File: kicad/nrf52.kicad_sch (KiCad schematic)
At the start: 22 parts, among them U1005 NRF52833-CJAA, Y1001 ECS-320-8-47B-7KM-TR, Y1002 Crystal

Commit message: unify module and board
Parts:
- renumbered AE1001 to AE1, C1014 to C46, C1015 to C47, C1016 to C48, C1017 to C49, C1018 to C50, C1019 to C51, C1020 to C52, C1021 to C53, C1022 to C54, C1023 to C55, C1024 to C56, C1025 to C57, C1026 to C58, C1027 to C59, C1028 to C60, L1003 to L3, L1004 to L4, L1005 to L5, U1005 to U15, Y1001 to Y3, Y1002 to Y4

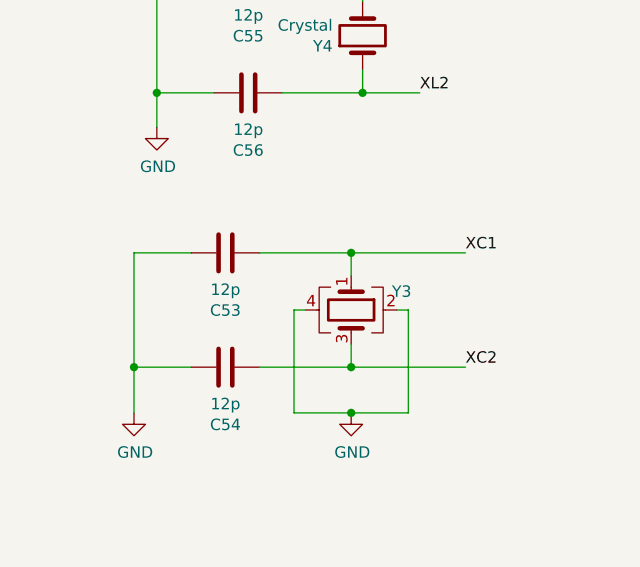
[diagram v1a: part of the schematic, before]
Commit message: move module parts to common library
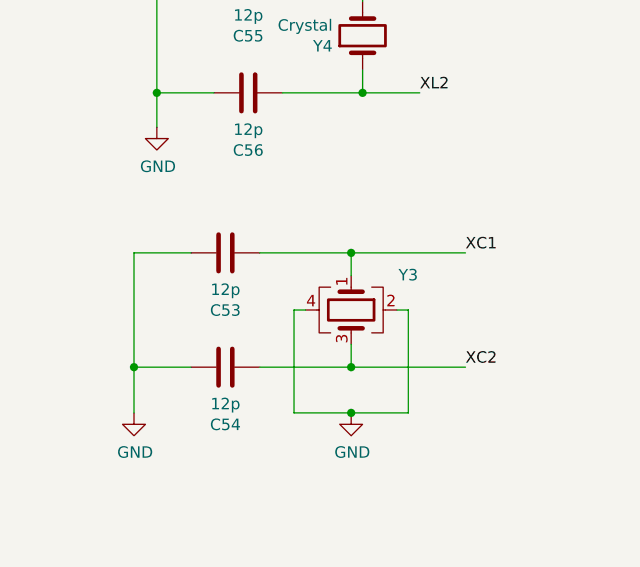
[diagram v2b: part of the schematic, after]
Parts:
- U15: symbol Riotee:NRF52833-CJAA -> riotee:NRF52833-CJAA
- Y3: symbol Riotee:ECS-320-8-47B-7KM-TR -> riotee:ECS-320-8-47B-7KM-TR
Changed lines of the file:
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@@
 	)
 	(symbol
-		(lib_id "Riotee:ECS-320-8-47B-7KM-TR")
+		(lib_id "riotee:ECS-320-8-47B-7KM-TR")
 		(at 255.27 59.69 270)
 		(unit 1)
@@
 		(fields_autoplaced yes)
 		(property "Reference" "Y3"
-			(at 260.8829 57.638 90)
+			(at 261.62 55.8098 90)
 			(effects
 				(font
@@
 			)
 		)
-		(property "Description" "32MHz, 8pF, 50R Crystal"
+		(property "Description" "Four pin crystal, GND on pins 2 and 4"
 			(at 255.27 59.69 0)
 			(effects
@@
 	)
 	(symbol
-		(lib_id "Riotee:NRF52833-CJAA")
+		(lib_id "riotee:NRF52833-CJAA")
 		(at 119.38 86.36 0)
 		(unit 1)

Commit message: resolve ERC
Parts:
- AE1: footprint Riotee:Texas_SWRA117D_2.4GHz_Left -> riotee:Texas_SWRA117D_2.4GHz_Left
- C46: footprint Riotee:C_0402_1005Metric -> riotee:C_0402_1005Metric; symbol Riotee:C -> Device:C
- C47, C48, C49, C50, C52, C53, C54, C55, C56, C58, C60: footprint Riotee:C_0201_0603Metric -> riotee:C_0201_0603Metric; symbol Riotee:C -> Device:C
- C51, C57, C59: footprint Riotee:RFSMD_0201_0603Metric -> riotee:RFSMD_0201_0603Metric; symbol Riotee:C -> Device:C
- L3, L4, L5: footprint Riotee:RFSMD_0201_0603Metric -> riotee:RFSMD_0201_0603Metric
- U15: footprint Riotee:NRF52833-CJAA -> riotee:NRF52833-CJAA
- Y3: footprint Riotee:ECS_ECX-1247B -> riotee:ECS_ECX-1247B
- Y4: footprint Riotee:ECX-12R -> riotee:ECX-12R

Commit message: resolve remaining import errors
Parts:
- C46: footprint riotee:C_0402_1005Metric -> Capacitor_SMD:C_0402_1005Metric
- C47, C48, C49, C50, C52, C53, C54, C55, C56, C58, C60: footprint riotee:C_0201_0603Metric -> Capacitor_SMD:C_0201_0603Metric
- L3, L4, L5: symbol Riotee:L -> Device:L
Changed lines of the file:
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@@
 	)
 	(symbol
-		(lib_id "Riotee:L")
+		(lib_id "Device:L")
 		(at 227.33 143.51 270)
 		(unit 1)
@@
 			)
 		)
-		(property "Datasheet" ""
+		(property "Datasheet" "~"
 			(at 227.33 143.51 0)
 			(effects
@@
 			)
 		)
-		(property "Description" "FIXED IND 5.6NH 350MA 400MOHM SM"
+		(property "Description" "Inductor"
 			(at 227.33 143.51 0)
 			(effects
@@
 			)
 		)
-		(property "Footprint" "riotee:C_0201_0603Metric"
+		(property "Footprint" "Capacitor_SMD:C_0201_0603Metric"
 			(at 61.2648 44.45 0)
 			(effects
@@
 			)
 		)
-		(property "Footprint" "riotee:C_0201_0603Metric"
+		(property "Footprint" "Capacitor_SMD:C_0201_0603Metric"
 			(at 237.49 54.3052 0)
 			(effects
@@
 			)
 		)
-		(property "Footprint" "riotee:C_0201_0603Metric"
+		(property "Footprint" "Capacitor_SMD:C_0201_0603Metric"
 			(at 237.49 67.0052 0)
 			(effects
@@
 			)
 		)
-		(property "Footprint" "riotee:C_0201_0603Metric"
+		(property "Footprint" "Capacitor_SMD:C_0201_0603Metric"
 			(at 240.03 23.8252 0)
 			(effects
@@
 			)
 		)
-		(property "Footprint" "riotee:C_0402_1005Metric"
+		(property "Footprint" "Capacitor_SMD:C_0402_1005Metric"
 			(at 21.2852 52.07 0)
 			(effects
@@
 			)
 		)
-		(property "Footprint" "riotee:C_0201_0603Metric"
+		(property "Footprint" "Capacitor_SMD:C_0201_0603Metric"
 			(at 51.1048 44.45 0)
 			(effects
@@
 			)
 		)
-		(property "Footprint" "riotee:C_0201_0603Metric"
+		(property "Footprint" "Capacitor_SMD:C_0201_0603Metric"
 			(at 254.3048 105.41 0)
 			(effects
@@
 	)
 	(symbol
-		(lib_id "Riotee:L")
+		(lib_id "Device:L")
 		(at 242.57 148.59 0)
 		(unit 1)
@@
 			)
 		)
-		(property "Datasheet" ""
+		(property "Datasheet" "~"
 			(at 242.57 148.59 0)
 			(effects
@@
 			)
 		)
-		(property "Description" "FIXED IND 2.7NH 500MA 200MOHM SM"
+		(property "Description" "Inductor"
 			(at 242.57 148.59 0)
 			(effects
@@
 			)
 		)
-		(property "Footprint" "riotee:C_0201_0603Metric"
+		(property "Footprint" "Capacitor_SMD:C_0201_0603Metric"
 			(at 40.9448 44.45 0)
 			(effects
@@
 	)
 	(symbol
-		(lib_id "Riotee:L")
+		(lib_id "Device:L")
 		(at 215.9 143.51 270)
 		(unit 1)
@@
 			)
 		)
-		(property "Datasheet" ""
+		(property "Datasheet" "~"
 			(at 215.9 143.51 0)
 			(effects
@@
 			)
 		)
-		(property "Description" "FIXED IND 3.9NH 400MA 300MOHM SM"
+		(property "Description" "Inductor"
 			(at 215.9 143.51 0)
 			(effects
@@
 			)
 		)
-		(property "Footprint" "riotee:C_0201_0603Metric"
+		(property "Footprint" "Capacitor_SMD:C_0201_0603Metric"
 			(at 268.2748 105.41 0)
 			(effects
@@
 			)
 		)
-		(property "Footprint" "riotee:C_0201_0603Metric"
+		(property "Footprint" "Capacitor_SMD:C_0201_0603Metric"
 			(at 236.5248 105.41 0)
 			(effects
@@
 			)
 		)
-		(property "Footprint" "riotee:C_0201_0603Metric"
+		(property "Footprint" "Capacitor_SMD:C_0201_0603Metric"
 			(at 240.03 36.5252 0)
 			(effects
@@
 			)
 		)
-		(property "Footprint" "riotee:C_0201_0603Metric"
+		(property "Footprint" "Capacitor_SMD:C_0201_0603Metric"
 			(at 30.7848 44.45 0)
 			(effects
